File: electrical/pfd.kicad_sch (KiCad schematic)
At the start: 14 parts

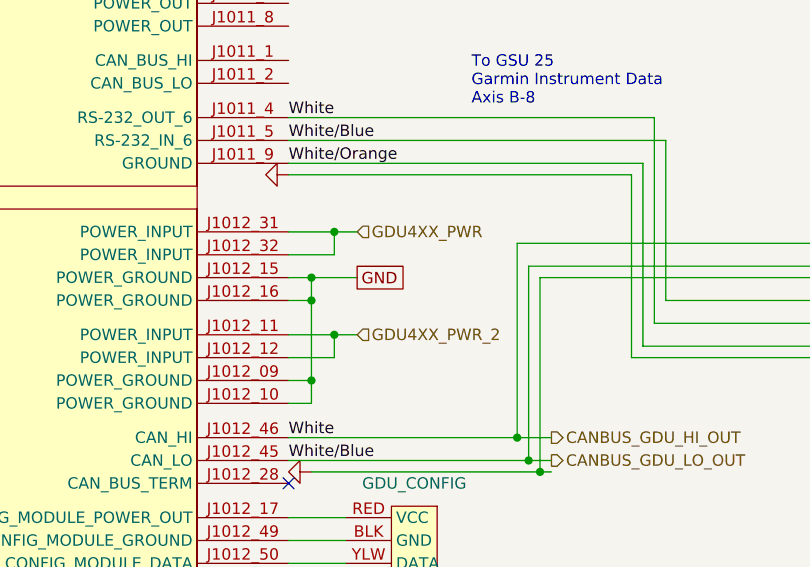
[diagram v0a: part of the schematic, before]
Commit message: Updated wiring to just do GDU Bat Lead leader. Also, keep pin 31 as effectively backup power like it was on G3X Touch
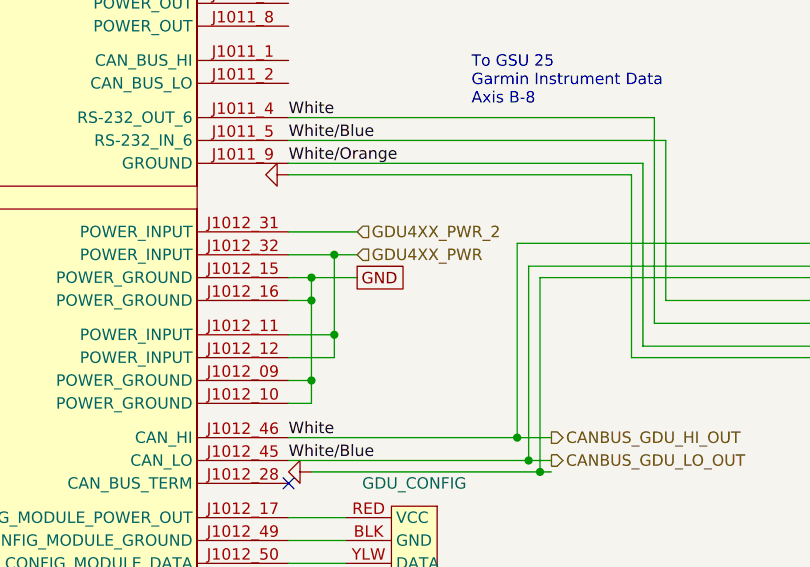
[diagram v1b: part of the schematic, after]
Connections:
- net GDU4XX_PWR: now also GDU116B.J1012_11 (POWER_INPUT), GDU116B.J1012_12 (POWER_INPUT); no longer GDU116B.J1012_31 (POWER_INPUT)
- net GDU4XX_PWR_2: now also GDU116B.J1012_31 (POWER_INPUT); no longer GDU116B.J1012_11 (POWER_INPUT), GDU116B.J1012_12 (POWER_INPUT)
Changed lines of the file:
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@@
 	(title_block
 		(title "PFD & ADAHRS")
-		(date "2026-08-01")
-		(rev "2.0.1")
+		(date "2026-08-18")
+		(rev "2.0.2")
 		(company "N877RV")
 	)
@@
 	)
 	(junction
+		(at 63.5 60.96)
+		(diameter 0)
+		(color 0 0 0 0)
+	)
+	(junction
 		(at 63.5 69.85)
 		(diameter 0)
@@
 	)
 	(junction
-		(at 63.5 58.42)
-		(diameter 0)
-		(color 0 0 0 0)
-	)
-	(junction
 		(at 60.96 66.04)
 		(diameter 0)
@@
 	(wire
 		(pts
-			(xy 63.5 60.96) (xy 63.5 58.42)
-		)
-		(stroke
-			(width 0)
-			(type default)
-		)
-	)
-	(wire
-		(pts
 			(xy 58.42 110.49) (xy 76.2 110.49)
 		)
@@
 	(wire
 		(pts
-			(xy 63.5 58.42) (xy 66.04 58.42)
+			(xy 58.42 58.42) (xy 66.04 58.42)
 		)
 		(stroke
@@
 	(wire
 		(pts
-			(xy 63.5 69.85) (xy 66.04 69.85)
+			(xy 63.5 60.96) (xy 66.04 60.96)
 		)
 		(stroke
@@
 	(wire
 		(pts
-			(xy 58.42 58.42) (xy 63.5 58.42)
-		)
-		(stroke
-			(width 0)
-			(type default)
-		)
-	)
-	(wire
-		(pts
 			(xy 161.29 170.18) (xy 167.64 170.18)
 		)
@@
 		(pts
 			(xy 66.04 223.52) (xy 66.04 224.79)
+		)
+		(stroke
+			(width 0)
+			(type default)
+		)
+	)
+	(wire
+		(pts
+			(xy 63.5 60.96) (xy 63.5 69.85)
 		)
 		(stroke
@@
 		)
 	)
-	(hierarchical_label "GDU4XX_PWR_2"
+	(hierarchical_label "GDU4XX_PWR"
 		(shape input)
-		(at 66.04 69.85 0)
+		(at 66.04 60.96 0)
 		(effects
 			(font
@@
 		)
 	)
-	(hierarchical_label "GDU4XX_PWR"
+	(hierarchical_label "GDU4XX_PWR_2"
 		(shape input)
 		(at 66.04 58.42 0)
